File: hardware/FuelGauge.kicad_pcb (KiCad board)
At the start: 2 copper layers, 112.3 x 69.6 mm, 35 parts, among them J1 Conn_01x10, J2 Conn_01x06, Q1 BC547, Q2 BC547, Q3 BC557, Q4 PHB55N03LT, U1 LM317L_TO92, U2 LM7805_TO220, U3 PIC12F1840-IP

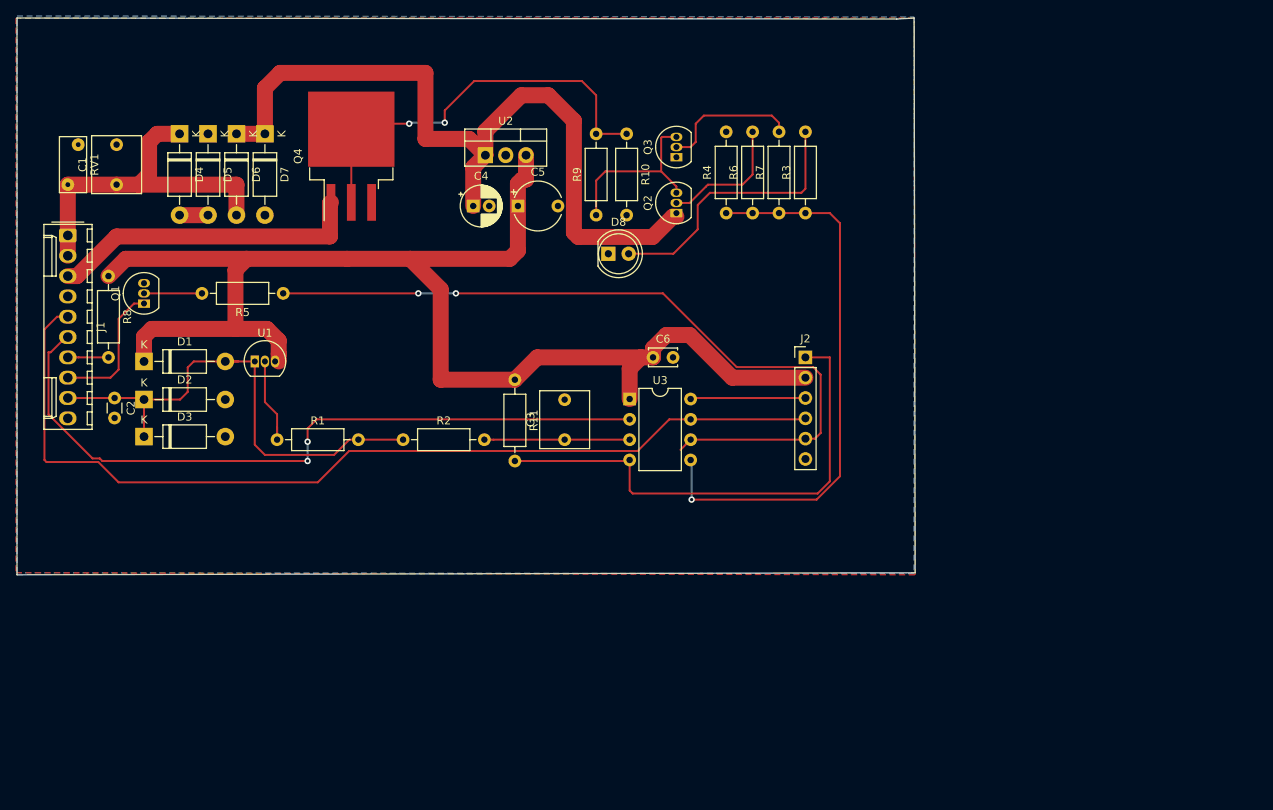
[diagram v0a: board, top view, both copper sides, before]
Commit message: Reroute to a smaller 49x81mm board
This re-lays out the board to a much smaller form factor with more intelligent routing. The track size for power nets is reduced
to 1.2mm which should be good for 2.7A max current. A number
of ground plane vias have been thrown in with little thought to
achieve better coverage.
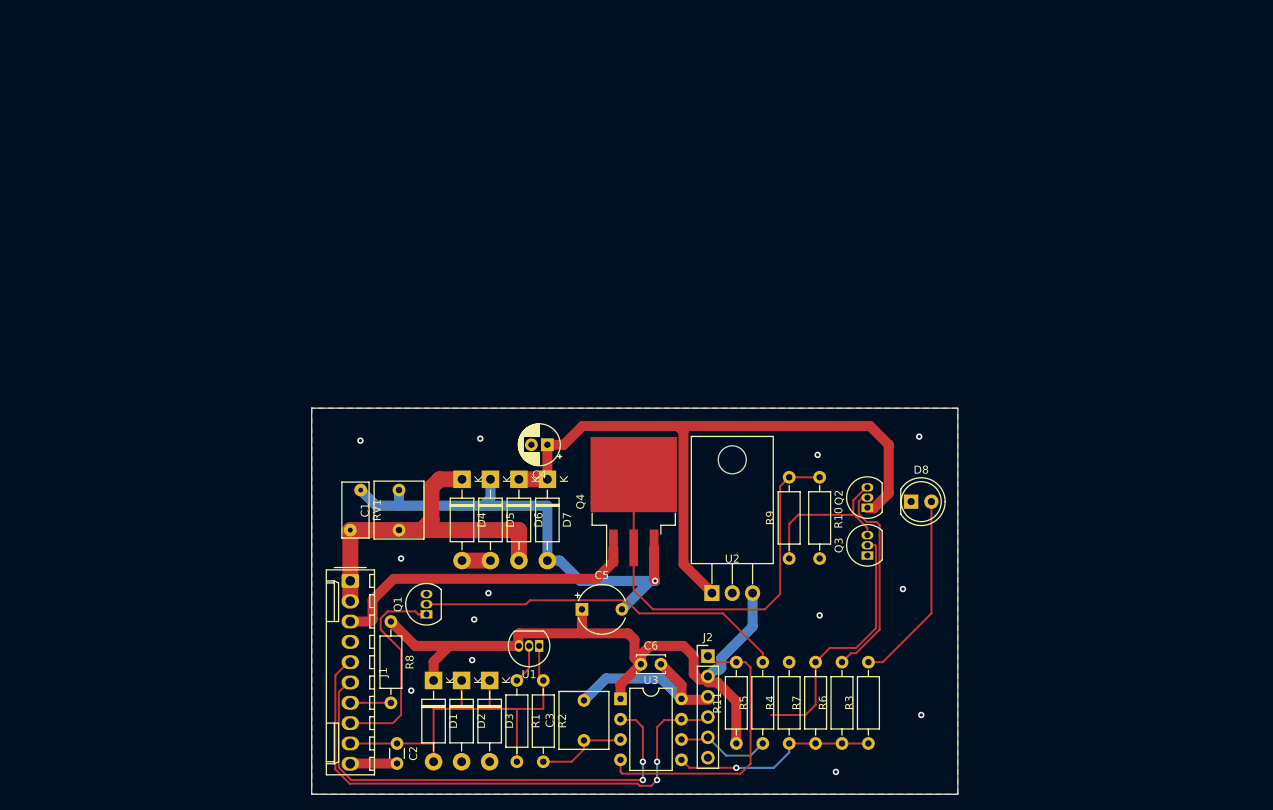
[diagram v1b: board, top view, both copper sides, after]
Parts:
- U2: footprint Package_TO_SOT_THT:TO-220-3_Vertical -> Package_TO_SOT_THT:TO-220-3_Horizontal_TabDown
- moved R5 82.2 mm to (112.3, 97.8), turned to 90 degrees
- moved R6 67.2 mm to (122.2, 97.8)
- moved R3 66.8 mm to (125.5, 97.8)
- moved R4 66.8 mm to (115.6, 97.8)
- moved R7 66.5 mm to (118.9, 97.8)
- moved U2 61.6 mm to (105.9, 79.0)
- moved C1 55.8 mm to (66.8, 71.1)
- moved C2 55.8 mm to (66.5, 97.8)
- moved J1 55.8 mm to (60.7, 77.5)
- moved RV1 55.8 mm to (60.7, 71.1)
- moved D4 55.8 mm to (74.7, 64.8)
- moved D5 55.8 mm to (78.2, 64.8)
- moved D6 55.8 mm to (81.8, 64.8)
- moved D7 55.8 mm to (85.3, 64.8)
- moved Q4 55.8 mm to (96.1, 67.6)
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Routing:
- net /Fuel Low: track 97.1 -> 11.8 mm, vias 2 -> 0
- net +5V: track 171.3 -> 86.7 mm
- net GND: track 14.4 -> 91.3 mm, vias 0 -> 14
- net /TX: track 119.5 -> 69.0 mm, vias 0 -> 2
- net /PWM Out: track 71.1 -> 25.7 mm
- net Net-(Q1-Pad2): track 7.24 -> 46.1 mm
- net /RX: track 90.6 -> 60.0 mm
- net /~MCLR~/VPP: track 62.6 -> 36.0 mm
- net Net-(Q3-Pad2): track 17.3 -> 32.1 mm
- net +12C: track 99.0 -> 84.7 mm
- net /Sender Input: track 64.1 -> 52.9 mm
- net Net-(D8-Pad2): track 34.4 -> 24.4 mm
- net Net-(Q2-Pad2): track 15.6 -> 25.5 mm
- net /Fuel LED K: track 17.1 -> 26.4 mm
- net /ADC In: track 18.2 -> 11.4 mm
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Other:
- board size 112.3 x 69.6 mm -> 80.8 x 48.3 mm
- net class Power: trace_width 2 -> 1.25

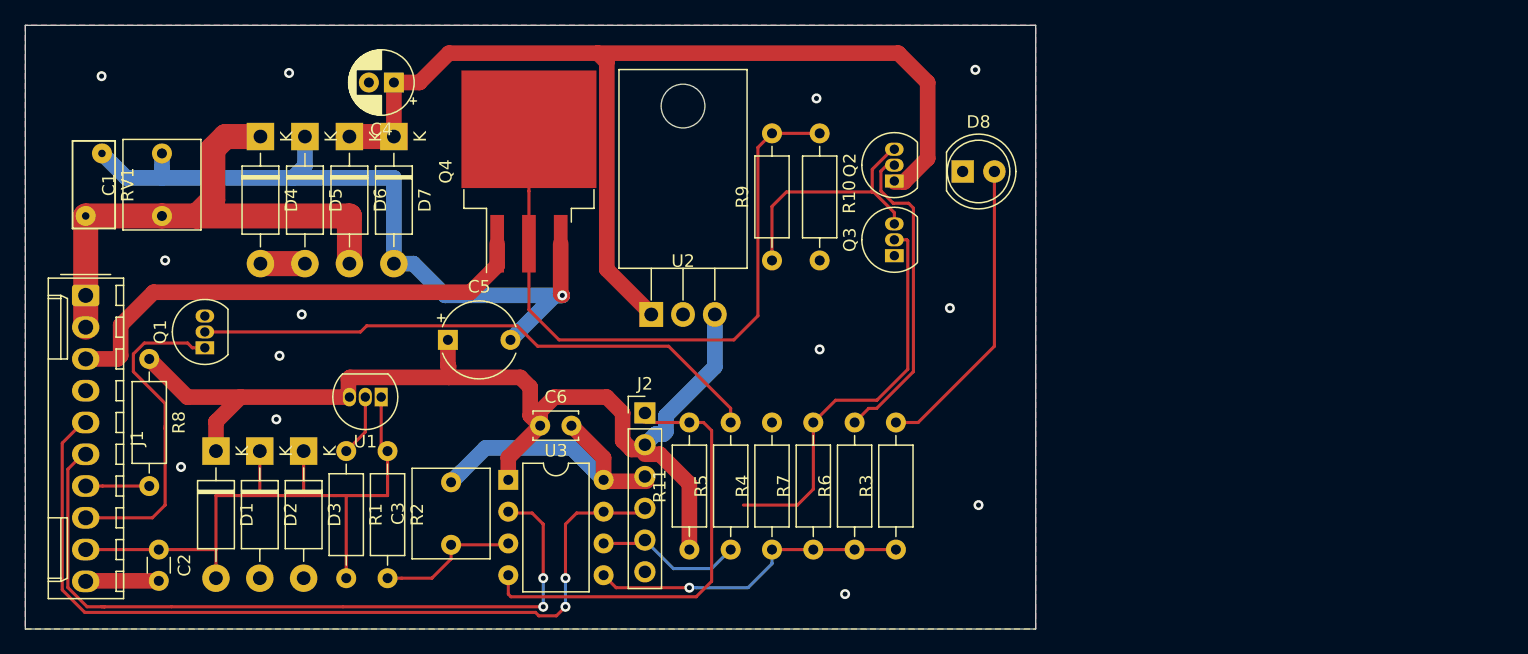
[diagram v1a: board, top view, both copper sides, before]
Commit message: Version 1.0 hardware
This change contains what is hoped to be 1.0 hardware. It removes the complex MOSFET driver for a simple direct drive
from the MCU. The LED has been removed as this appears to
provide little value as the VDO test guage uses 65% to 98% duty
cycle to cover 0% to 100% which is virtually imperceptible.

A simple transistor driver for a low fuel warning LED or lamp has
been included. This should work with a 12V LED indicator lamp.

Tests:
 - Run a full ERC on schematic and DRC on the PCB
 - Check mechanical fit with a 1:1 printout against the Hammond
   1691ABK case
 - Check new MOSFET driver with VDO fuel gauge and calibrate
   output map. MOSFET turn on time seems to be about 1uS
   which should be OK given low current.
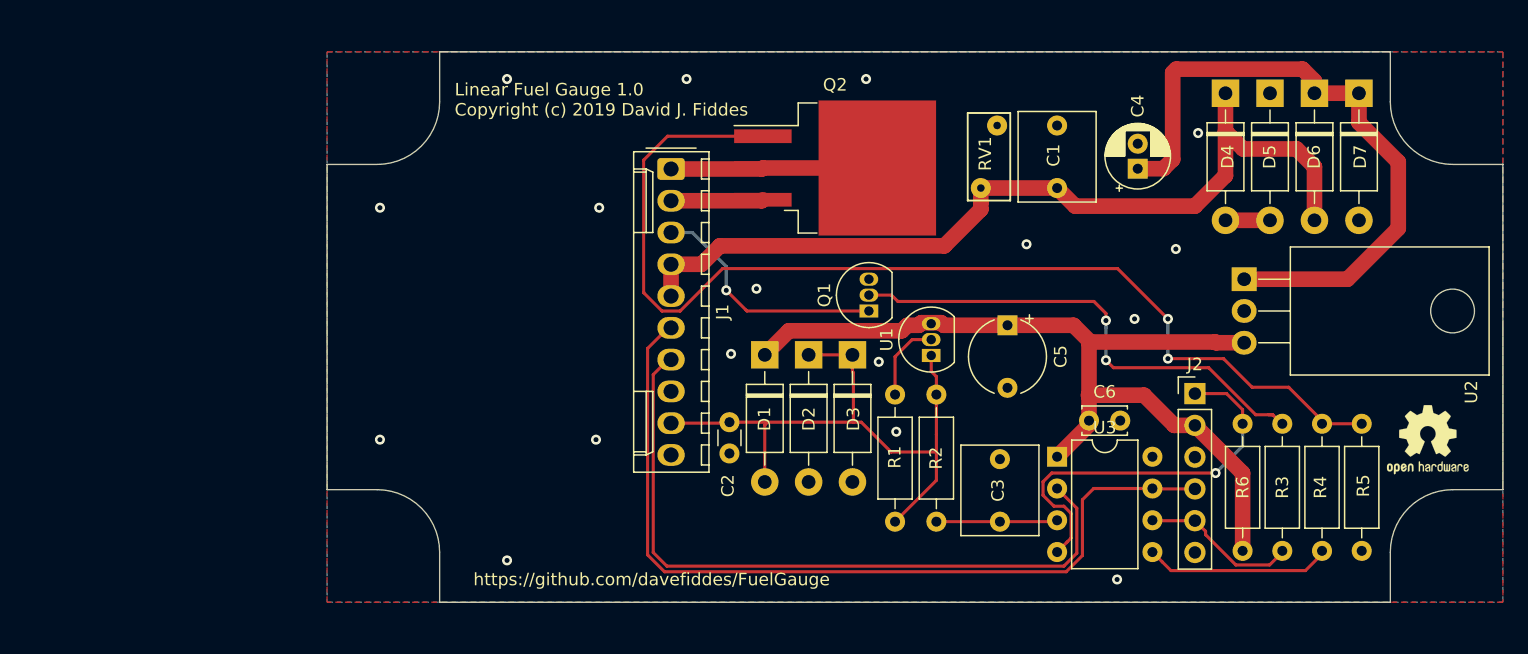
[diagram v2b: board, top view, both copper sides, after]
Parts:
- removed D8: LED, LED_THT:LED_D5.0mm_Clear
- removed Q3: BC557, Package_TO_SOT_THT:TO-92_Inline
- removed Q4: PHB55N03LT, Package_TO_SOT_SMD:TO-263-3_TabPin2
- removed R10: 4K7, Resistor_THT:R_Axial_DIN0207_L6.3mm_D2.5mm_P10.16mm_Horizontal
- removed R11: 10K, Resistor_THT:R_Axial_DIN0207_L6.3mm_D2.5mm_P10.16mm_Horizontal
- removed R7: 1K, Resistor_THT:R_Axial_DIN0207_L6.3mm_D2.5mm_P10.16mm_Horizontal
- removed R8: 330R, Resistor_THT:R_Axial_DIN0207_L6.3mm_D2.5mm_P10.16mm_Horizontal
- removed R9: 10R, Resistor_THT:R_Axial_DIN0207_L6.3mm_D2.5mm_P10.16mm_Horizontal
- added Logo1: OSHW-Logo2_7.3x6mm_SilkScreen, Symbol:OSHW-Logo2_7.3x6mm_SilkScreen, F.Cu at (168.0, 89.0)
- Q2: value BC547 -> PHB55N03LT; footprint Package_TO_SOT_THT:TO-92_Inline -> Package_TO_SOT_SMD:TO-263-3_TabPin2
- R3: value 330R -> 1K
- R4: value 10K -> 10R
- R5: value 1K -> 4K7
- R6: value 1K -> 10K
- moved D4 77.2 mm to (151.8, 61.3)
- moved D6 77.2 mm to (158.9, 61.3)
- moved D5 77.2 mm to (155.4, 61.3)
- moved D7 77.2 mm to (162.5, 61.3)
- moved C1 71.6 mm to (138.4, 68.9)
- moved RV1 71.6 mm to (132.3, 68.9)
- moved C4 59.9 mm to (144.8, 67.3), turned to 90 degrees
- moved Q1 53.2 mm to (123.3, 78.7)
- moved R5 51.4 mm to (162.7, 87.7), turned to 270 degrees
- moved J1 47.9 mm to (107.5, 67.4)
- moved U2 47.5 mm to (153.3, 76.2), turned to 270 degrees
- moved C2 46.7 mm to (112.2, 87.6)
- moved C5 44.7 mm to (134.4, 79.9), turned to 270 degrees
- moved D1 44.5 mm to (115.0, 82.2)
- moved D2 44.5 mm to (118.5, 82.2)
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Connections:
- C4 pad 1: +12C -> Net-(C4-Pad1)
- D6 pad 1: +12C -> Net-(C4-Pad1)
- D7 pad 1: +12C -> Net-(C4-Pad1)
- J1 pad 1: +12V -> /Gauge Output
- J1 pad 2: +12V -> GND
- J1 pad 3: /Gauge Output -> /Fuel Low Output
- J1 pad 4: GND -> +12V
- J1 pad 5: /TX -> +12V
- J1 pad 6: /RX -> /TX
- J1 pad 7: /Fuel LED A -> /RX
- J1 pad 8: /Fuel LED K -> GND
- Q1 pad 1: /Fuel LED K -> /Fuel Low Output
- Q2 pad 1: +12C -> Net-(Q2-Pad1)
- Q2 pad 2: Net-(Q2-Pad2) -> /Gauge Output
- Q2 pad 3: Net-(Q2-Pad3) -> GND
- R3 pad 1: /PWM Out -> /Fuel Low
- R3 pad 2: Net-(D8-Pad2) -> Net-(Q1-Pad2)
- R4 pad 2: GND -> Net-(Q2-Pad1)
- R5 pad 1: /Fuel Low -> Net-(Q2-Pad1)
- R5 pad 2: Net-(Q1-Pad2) -> GND
- R6 pad 1: /PWM Out -> +5V
- R6 pad 2: Net-(Q2-Pad2) -> /~MCLR~/VPP
- U2 pad 1: +12C -> Net-(C4-Pad1)
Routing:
- net Net-(Q2-Pad1): track 0.00 -> 88.0 mm, vias 0 -> 2
- net +12C: track 84.7 -> 0.00 mm
- net GND: track 91.3 -> 7.65 mm, vias 14 -> 17
- net Net-(Q4-Pad2): track 53.4 -> 0.00 mm
- net Net-(C4-Pad1): track 0.00 -> 52.5 mm
- net Net-(Q3-Pad2): track 32.1 -> 0.00 mm
- net +12V: track 43.9 -> 71.1 mm
- net /Fuel LED K: track 26.4 -> 0.00 mm
- net Net-(Q2-Pad2): track 25.5 -> 0.00 mm
- net Net-(D8-Pad2): track 24.4 -> 0.00 mm
- net /Gauge Output: track 39.2 -> 16.5 mm
- net /Fuel Low Output: track 0.00 -> 19.8 mm, vias 0 -> 1
- net Net-(Q2-Pad3): track 19.6 -> 0.00 mm
- net +5V: track 86.7 -> 71.5 mm
- net /PWM Out: track 25.7 -> 15.1 mm, vias 1 -> 0
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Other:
- board size 80.8 x 48.3 mm -> 94 x 44 mm
- board text added: "Linear Fuel Gauge 1.0 Copyright (c) 2019 David J. Fiddes"
- board text added: "PCB to fit Hammond 1591ABK enclosure"
- board text added: "https://github.com/davefiddes/FuelGauge"
